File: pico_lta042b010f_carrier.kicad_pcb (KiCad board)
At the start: 2 copper layers, 100 x 52 mm, 31 parts, among them J1 LTA042B010F_FFC_36P_0.5mm, J2 USB-C 5V INPUT, J3 CCFL_INVERTER_13V8, U1 RaspberryPi_Pico_2W, U3 MC34063AD

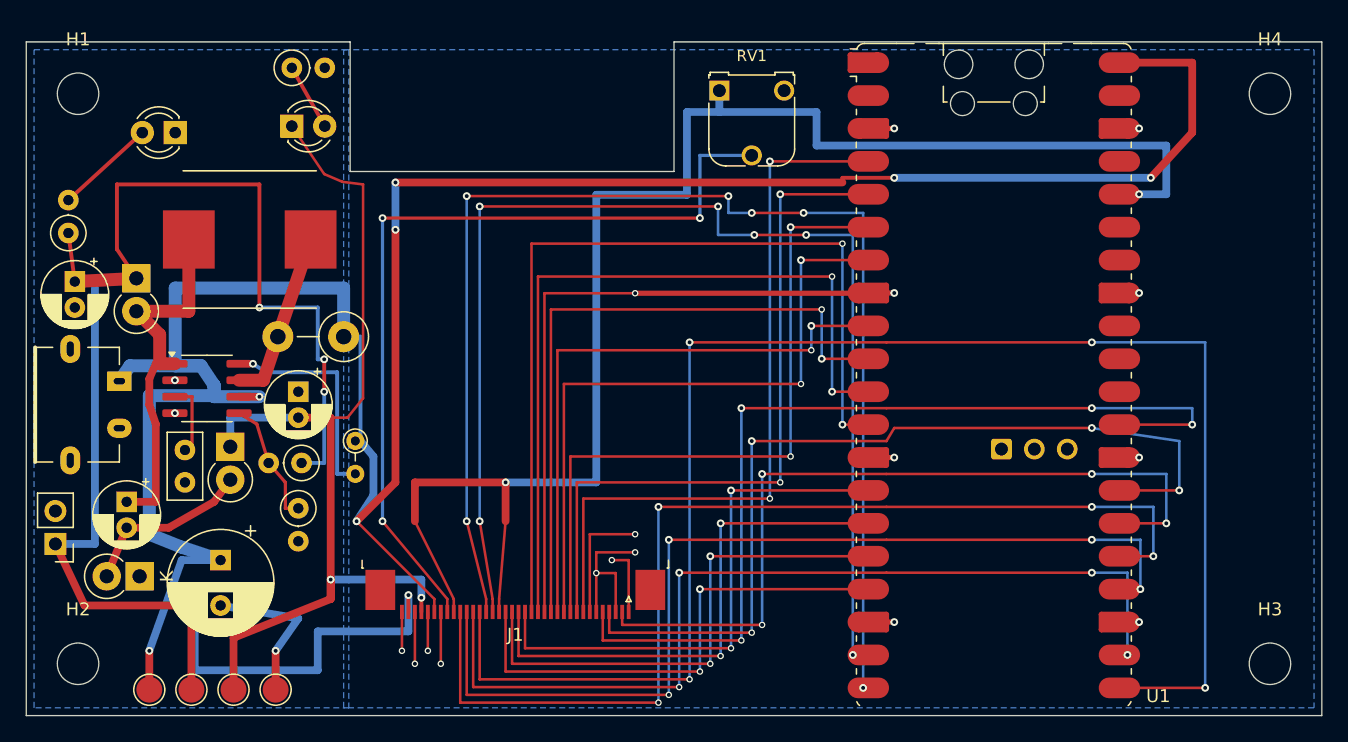
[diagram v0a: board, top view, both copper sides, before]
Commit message: Tighten PCB design rules and edge margins
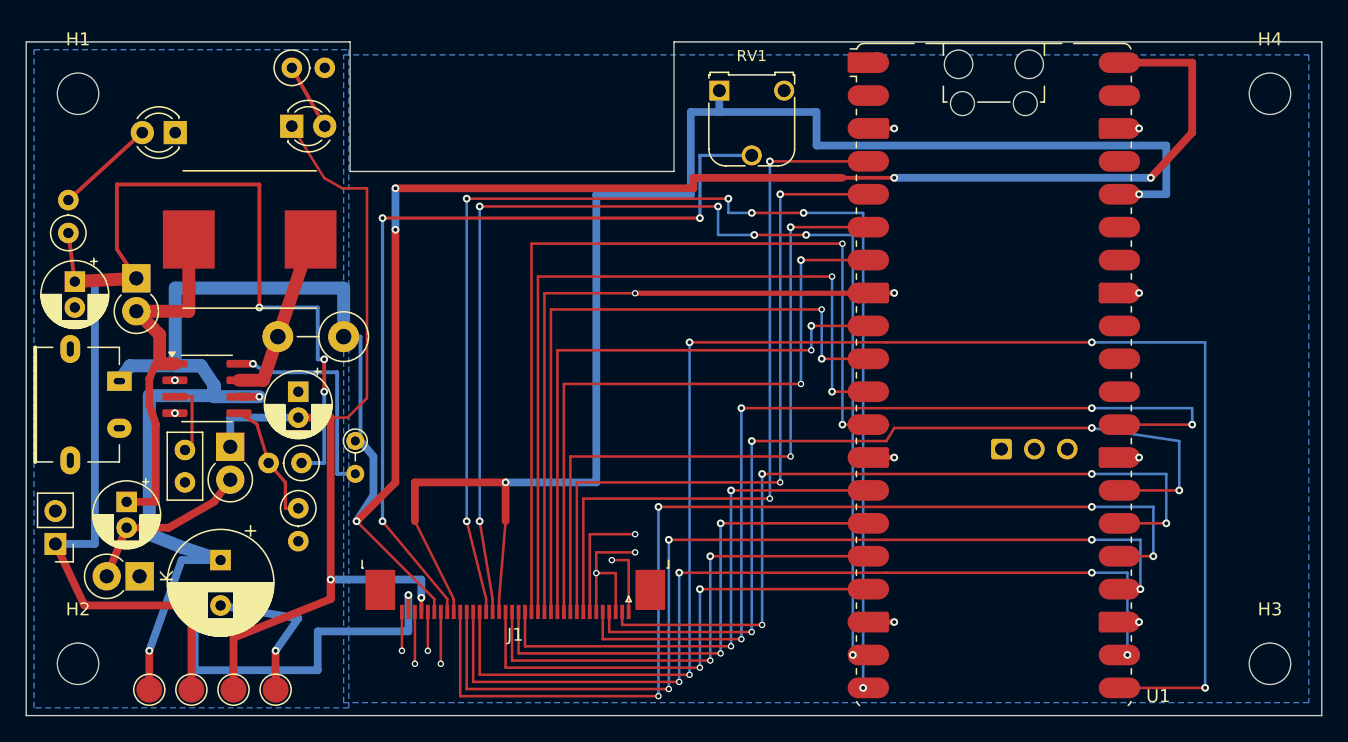
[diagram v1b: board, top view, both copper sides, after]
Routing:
- net LCD_R0: track 82.0 -> 81.0 mm
- net LCD_R1: track 75.8 -> 74.9 mm
- net LCD_R2: track 72.1 -> 71.3 mm
- net LCD_R3: track 120.5 -> 119.8 mm
- net LCD_G0: track 39.0 -> 38.4 mm
- net -13V8: track 76.9 -> 77.4 mm
- net LCD_G1: track 39.8 -> 39.3 mm
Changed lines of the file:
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@@
 	)
 	(segment
-		(start 63 10.85)
-		(end 63 10.49)
-		(width 0.3)
+		(start 28.5 11.3)
+		(end 51.5 11.3)
+		(width 0.6)
+		(layer "F.Cu")
+		(net 2)
+	)
+	(segment
+		(start 51.5 11.3)
+		(end 51.5 10.49)
+		(width 0.6)
 		(layer "F.Cu")
 		(net 2)
@@
 	)
 	(segment
-		(start 28.5 10.85)
-		(end 63 10.85)
+		(start 51.5 10.49)
+		(end 63 10.49)
 		(width 0.6)
 		(layer "F.Cu")
@@
 	)
 	(via
-		(at 28.5 10.85)
+		(at 28.5 11.3)
 		(size 0.6)
 		(drill 0.3)
@@
 	(segment
 		(start 28.5 14.5)
-		(end 28.5 10.85)
+		(end 28.5 11.3)
 		(width 0.6)
 		(layer "B.Cu")
@@
 	)
 	(segment
-		(start 24.4 10.8)
-		(end 23 10.2)
+		(start 24.4 11.3)
+		(end 23 10.5)
 		(width 0.2)
 		(layer "F.Cu")
@@
 	)
 	(segment
-		(start 23 10.2)
+		(start 23 10.5)
 		(end 20.5 6.5)
 		(width 0.2)
@@
 	)
 	(segment
-		(start 26 11)
-		(end 24.4 10.8)
+		(start 26.3 11.3)
+		(end 24.4 11.3)
 		(width 0.2)
 		(layer "F.Cu")
@@
 	(segment
 		(start 24.8 29)
-		(end 26 27.5)
+		(end 26.3 27.5)
 		(width 0.2)
 		(layer "F.Cu")
@@
 	)
 	(segment
-		(start 26 27.5)
-		(end 26 11)
+		(start 26.3 27.5)
+		(end 26.3 11.3)
 		(width 0.2)
 		(layer "F.Cu")
@@
 	(segment
 		(start 44 11.8)
-		(end 51 11.8)
+		(end 51.3 11.8)
 		(width 0.6)
 		(layer "B.Cu")
@@
 	)
 	(segment
-		(start 51 5.41)
+		(start 51.3 5.41)
 		(end 53.5 5.41)
 		(width 0.6)
@@
 	)
 	(segment
-		(start 51 11.8)
-		(end 51 5.41)
+		(start 51.3 11.8)
+		(end 51.3 5.41)
 		(width 0.6)
 		(layer "B.Cu")
@@
 	)
 	(segment
-		(start 45 45.6)
-		(end 56 45.6)
+		(start 45 45.55)
+		(end 56 45.55)
 		(width 0.2)
 		(layer "F.Cu")
@@
 	(segment
 		(start 45 44)
-		(end 45 45.6)
+		(end 45 45.55)
 		(width 0.2)
 		(layer "F.Cu")
@@
 	)
 	(via
-		(at 56 45.6)
+		(at 56 45.55)
 		(size 0.5)
 		(drill 0.3)
@@
 	)
 	(segment
-		(start 56 45.6)
+		(start 56 45.55)
 		(end 56 30.81)
 		(width 0.2)
@@
 	)
 	(segment
-		(start 44.5 46.2)
-		(end 55.2 46.2)
+		(start 44.5 46.1)
+		(end 55.2 46.1)
 		(width 0.2)
 		(layer "F.Cu")
@@
 	(segment
 		(start 44.5 44)
-		(end 44.5 46.2)
+		(end 44.5 46.1)
 		(width 0.2)
 		(layer "F.Cu")
@@
 	)
 	(via
-		(at 55.2 46.2)
+		(at 55.2 46.1)
 		(size 0.5)
 		(drill 0.3)
@@
 	)
 	(segment
-		(start 55.2 46.2)
+		(start 55.2 46.1)
 		(end 55.2 28.27)
 		(width 0.2)
@@
 	)
 	(segment
-		(start 38.5 46.8)
-		(end 54.4 46.8)
+		(start 38.5 46.65)
+		(end 54.4 46.65)
 		(width 0.2)
 		(layer "F.Cu")
@@
 	(segment
 		(start 38.5 44)
-		(end 38.5 46.8)
+		(end 38.5 46.65)
 		(width 0.2)
 		(layer "F.Cu")
@@
 	)
 	(via
-		(at 54.4 46.8)
+		(at 54.4 46.65)
 		(size 0.5)
 		(drill 0.3)
@@
 	)
 	(segment
-		(start 54.4 46.8)
+		(start 54.4 46.65)
 		(end 54.4 34.62)
 		(width 0.2)
@@
 	)
 	(segment
-		(start 38 47.4)
-		(end 53.6 47.4)
+		(start 38 47.2)
+		(end 53.6 47.2)
 		(width 0.2)
 		(layer "F.Cu")
@@
 	(segment
 		(start 38 44)
-		(end 38 47.4)
+		(end 38 47.2)
 		(width 0.2)
 		(layer "F.Cu")
@@
 	)
 	(via
-		(at 53.6 47.4)
+		(at 53.6 47.2)
 		(size 0.5)
 		(drill 0.3)
@@
 	)
 	(segment
-		(start 53.6 47.4)
+		(start 53.6 47.2)
 		(end 53.6 37.16)
 		(width 0.2)
@@
 	)
 	(segment
-		(start 37.5 48)
-		(end 52.8 48)
+		(start 37.5 47.75)
+		(end 52.8 47.75)
 		(width 0.2)
 		(layer "F.Cu")
@@
 	(segment
 		(start 37.5 44)
-		(end 37.5 48)
+		(end 37.5 47.75)
 		(width 0.2)
 		(layer "F.Cu")
@@
 	)
 	(via
-		(at 52.8 48)
+		(at 52.8 47.75)
 		(size 0.5)
 		(drill 0.3)
@@
 	)
 	(segment
-		(start 52.8 48)
+		(start 52.8 47.75)
 		(end 52.8 39.7)
 		(width 0.2)
@@
 	(segment
 		(start 37 44)
-		(end 37 48.6)
+		(end 37 48.3)
 		(width 0.2)
 		(layer "F.Cu")
@@
 	)
 	(segment
-		(start 37 48.6)
-		(end 52 48.6)
+		(start 37 48.3)
+		(end 52 48.3)
 		(width 0.2)
 		(layer "F.Cu")
@@
 	)
 	(via
-		(at 52 48.6)
+		(at 52 48.3)
 		(size 0.5)
 		(drill 0.3)
@@
 	)
 	(segment
-		(start 52 48.6)
+		(start 52 48.3)
 		(end 52 42.24)
 		(width 0.2)
@@
 	)
 	(segment
-		(start 34 11.9)
-		(end 54.2 11.9)
+		(start 34 12.1)
+		(end 54.2 12.1)
 		(width 0.2)
 		(layer "F.Cu")
@@
 	)
 	(via
-		(at 34 11.9)
+		(at 34 12.1)
 		(size 0.6)
 		(drill 0.3)
@@
 	)
 	(via
-		(at 54.2 11.9)
+		(at 54.2 12.1)
 		(size 0.6)
 		(drill 0.3)
@@
 	)
 	(segment
-		(start 54.2 11.9)
+		(start 54.2 12.1)
 		(end 54.2 13.2)
 		(width 0.2)
@@
 	(segment
 		(start 34 37)
-		(end 34 11.9)
+		(end 34 12.1)
 		(width 0.2)
 		(layer "B.Cu")
@@
 	(segment
 		(start 35 44)
-		(end 35 49.2)
+		(end 35 48.85)
 		(width 0.2)
 		(layer "F.Cu")
@@
 	)
 	(segment
-		(start 35 49.2)
-		(end 51.2 49.2)
+		(start 35 48.85)
+		(end 51.2 48.85)
 		(width 0.2)
 		(layer "F.Cu")
@@
 	)
 	(via
-		(at 51.2 49.2)
+		(at 51.2 48.85)
 		(size 0.5)
 		(drill 0.3)
@@
 	)
 	(segment
-		(start 51.2 49.2)
+		(start 51.2 48.85)
 		(end 51.2 23.19)
 		(width 0.2)
@@
 	(segment
 		(start 34.5 44)
-		(end 34.5 49.8)
+		(end 34.5 49.4)
 		(width 0.2)
 		(layer "F.Cu")
@@
 	)
 	(segment
-		(start 34.5 49.8)
-		(end 50.4 49.8)
+		(start 34.5 49.4)
+		(end 50.4 49.4)
 		(width 0.2)
 		(layer "F.Cu")
@@
 	)
 	(via
-		(at 50.4 49.8)
+		(at 50.4 49.4)
 		(size 0.5)
 		(drill 0.3)
@@
 	)
 	(segment
-		(start 50.4 49.8)
+		(start 50.4 49.4)
 		(end 50.4 40.97)
 		(width 0.2)
@@
 	(segment
 		(start 34 44)
-		(end 34 50.4)
+		(end 34 49.95)
 		(width 0.2)
 		(layer "F.Cu")
@@
 	)
 	(segment
-		(start 34 50.4)
-		(end 49.6 50.4)
+		(start 34 49.95)
+		(end 49.6 49.95)
 		(width 0.2)
 		(layer "F.Cu")
@@
 	)
 	(via
-		(at 49.6 50.4)
+		(at 49.6 49.95)
 		(size 0.5)
 		(drill 0.3)
@@
 	)
 	(segment
-		(start 49.6 50.4)
+		(start 49.6 49.95)
 		(end 49.6 38.43)
 		(width 0.2)
@@
 	)
 	(segment
-		(start 33.5 51)
-		(end 48.8 51)
+		(start 33.5 50.5)
+		(end 48.8 50.5)
 		(width 0.2)
 		(layer "F.Cu")
@@
 	(segment
 		(start 33.5 44)
-		(end 33.5 51)
+		(end 33.5 50.5)
 		(width 0.2)
 		(layer "F.Cu")
@@
 	)
 	(via
-		(at 48.8 51)
+		(at 48.8 50.5)
 		(size 0.5)
 		(drill 0.3)
@@
 	)
 	(segment
-		(start 48.8 51)
+		(start 48.8 50.5)
 		(end 48.8 35.89)
 		(width 0.2)
@@
 		(polygon
 			(pts
-				(xy 24.5 0.6) (xy 99.4 0.6) (xy 99.4 51.4) (xy 24.5 51.4)
+				(xy 24.5 1) (xy 99 1) (xy 99 51) (xy 24.5 51)
 			)
 		)

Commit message: Add dual-layer thermal ground pours
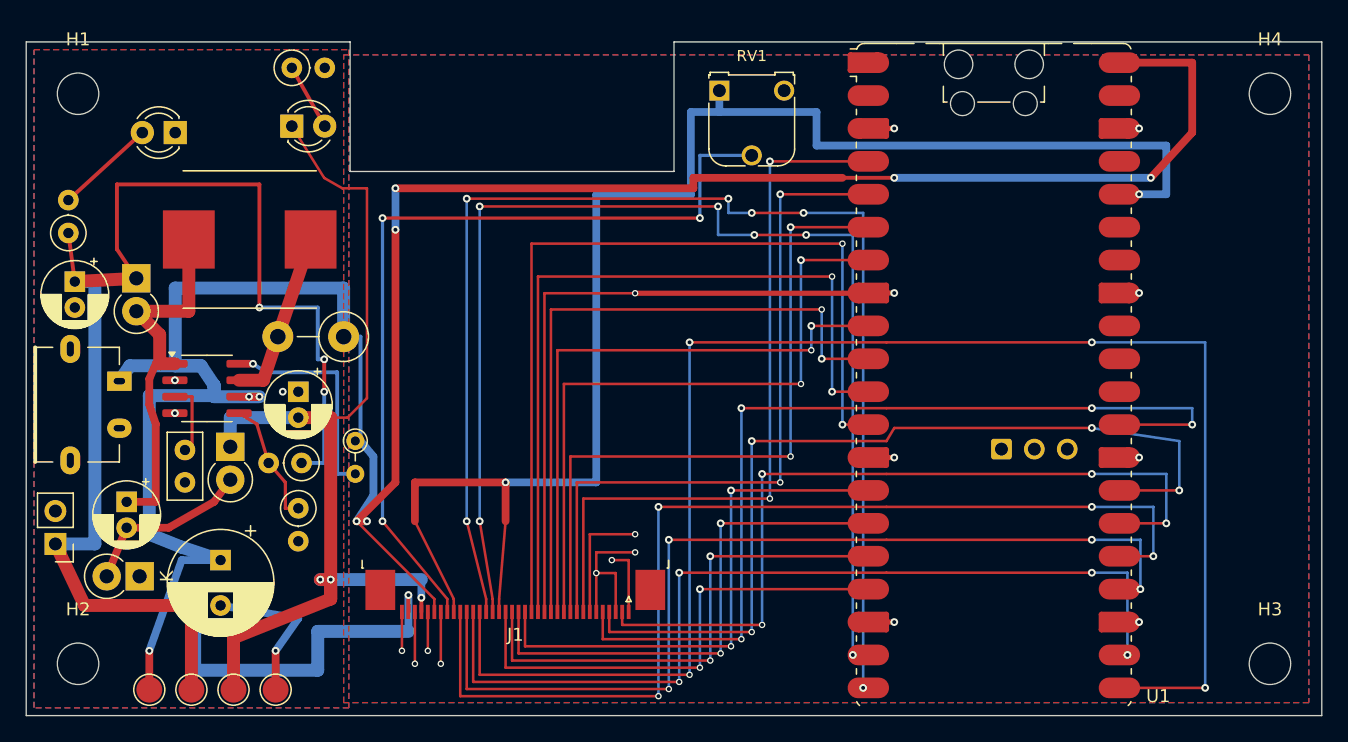
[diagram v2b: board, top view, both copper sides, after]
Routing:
- net +5V: track 203.2 -> 205.6 mm, vias 7 -> 9
- net +13V8: track 130.6 -> 132.2 mm, vias 5 -> 6
- net -13V8: track 77.4 -> 79.0 mm, vias 2 -> 3
- net GND: vias 20 -> 21
- added copper zone on F.Cu, net GND
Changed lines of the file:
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@@
+	)
+	(via
+		(at 19.8 27)
+		(size 0.6)
+		(drill 0.3)
+		(layers "F.Cu" "B.Cu")
+		(net 1)
 	)
 	(via
@@
 	)
 	(segment
+		(start 18 27.385)
+		(end 17.2 27.385)
+		(width 0.6)
+		(layer "F.Cu")
+		(net 2)
+	)
+	(segment
 		(start 28.5 11.3)
 		(end 51.5 11.3)
@@
 		(start 18 27.385)
 		(end 16.425 27.385)
+		(width 0.6)
+		(layer "F.Cu")
+		(net 2)
+	)
+	(segment
+		(start 25.5 37)
+		(end 26.3 37)
 		(width 0.6)
 		(layer "F.Cu")
@@
 	)
 	(via
+		(at 17.2 27.385)
+		(size 0.6)
+		(drill 0.3)
+		(layers "F.Cu" "B.Cu")
+		(net 2)
+	)
+	(via
 		(at 86.8 10.49)
+		(size 0.6)
+		(drill 0.3)
+		(layers "F.Cu" "B.Cu")
+		(net 2)
+	)
+	(via
+		(at 26.3 37)
 		(size 0.6)
 		(drill 0.3)
@@
 	)
 	(segment
+		(start 25.5 37)
+		(end 26.3 37)
+		(width 0.6)
+		(layer "B.Cu")
+		(net 2)
+	)
+	(segment
 		(start 13.5 25)
 		(end 14.5 26.5)
@@
 		(start 4.5 43.5)
 		(end 12.75 43.5)
-		(width 0.6)
+		(width 1)
 		(layer "F.Cu")
 		(net 3)
@@
 	)
 	(segment
+		(start 13 42.7)
+		(end 12.2 42.7)
+		(width 1)
+		(layer "F.Cu")
+		(net 3)
+	)
+	(segment
 		(start 3.75 18.5)
 		(end 3.25 14.75)
@@
 		(start 13 42.7)
 		(end 12.75 43.5)
-		(width 0.6)
+		(width 1)
 		(layer "F.Cu")
 		(net 3)
@@
 		(start 2.25 38.75)
 		(end 4.5 43.5)
-		(width 0.6)
+		(width 1)
 		(layer "F.Cu")
 		(net 3)
@@
 		(start 12.75 43.5)
 		(end 12.75 50)
-		(width 0.6)
+		(width 1)
 		(layer "F.Cu")
 		(net 3)
@@
 	)
 	(via
+		(at 12.2 42.7)
+		(size 0.6)
+		(drill 0.3)
+		(layers "F.Cu" "B.Cu")
+		(net 3)
+	)
+	(via
 		(at 18 20.5)
 		(size 0.6)
@@
 		(start 13 48.5)
 		(end 13 42.7)
-		(width 0.6)
+		(width 1)
 		(layer "B.Cu")
 		(net 3)
@@
 		(start 29.5 45.5)
 		(end 22.5 45.5)
-		(width 0.6)
+		(width 1)
+		(layer "B.Cu")
+		(net 3)
+	)
+	(segment
+		(start 13 42.7)
+		(end 12.2 42.7)
+		(width 1)
 		(layer "B.Cu")
 		(net 3)
@@
 		(start 5.3 38.75)
 		(end 2.25 38.75)
-		(width 0.6)
+		(width 1)
 		(layer "B.Cu")
 		(net 3)
@@
 		(start 3.75 18.5)
 		(end 5.3 18.5)
-		(width 0.6)
+		(width 1)
 		(layer "B.Cu")
 		(net 3)
@@
 		(start 22.5 45.5)
 		(end 22.5 48.5)
-		(width 0.6)
+		(width 1)
 		(layer "B.Cu")
 		(net 3)
@@
 		(start 5.3 18.5)
 		(end 5.3 38.75)
-		(width 0.6)
+		(width 1)
 		(layer "B.Cu")
 		(net 3)
@@
 		(start 22.5 48.5)
 		(end 13 48.5)
-		(width 0.6)
+		(width 1)
 		(layer "B.Cu")
 		(net 3)
@@
 		(start 23.5 43)
 		(end 16 46)
-		(width 0.6)
+		(width 1)
 		(layer "F.Cu")
 		(net 4)
@@
 		(start 23.5 29)
 		(end 23.5 43)
-		(width 0.6)
+		(width 1)
 		(layer "F.Cu")
 		(net 4)
@@
 		(start 21 29)
 		(end 23.5 29)
-		(width 0.6)
+		(width 1)
 		(layer "F.Cu")
 		(net 4)
@@
 		(start 16 46)
 		(end 16 50)
-		(width 0.6)
+		(width 1)
+		(layer "F.Cu")
+		(net 4)
+	)
+	(segment
+		(start 23.5 41.5)
+		(end 22.7 41.5)
+		(width 1)
 		(layer "F.Cu")
 		(net 4)
@@
 		(start 23.5 41.5)
 		(end 23.5 43)
-		(width 0.6)
+		(width 1)
 		(layer "F.Cu")
 		(net 4)
@@
 	)
 	(via
+		(at 22.7 41.5)
+		(size 0.6)
+		(drill 0.3)
+		(layers "F.Cu" "B.Cu")
+		(net 4)
+	)
+	(via
 		(at 23.5 41.5)
 		(size 0.6)
@@
 		(start 15.75 31.25)
 		(end 15.75 29)
-		(width 0.6)
+		(width 1)
 		(layer "B.Cu")
 		(net 4)
@@
 		(start 15.75 29)
 		(end 21 29)
-		(width 0.6)
+		(width 1)
 		(layer "B.Cu")
 		(net 4)
@@
 		(start 30.5 41.5)
 		(end 23.5 41.5)
-		(width 0.6)
+		(width 1)
+		(layer "B.Cu")
+		(net 4)
+	)
+	(segment
+		(start 23.5 41.5)
+		(end 22.7 41.5)
+		(width 1)
 		(layer "B.Cu")
 		(net 4)
@@
 		(net 1)
 		(net_name "GND")
-		(layer "B.Cu")
-		(name "LOGIC_GND")
+		(layer "F.Cu")
+		(name "POWER_STAGE_GND_F")
 		(hatch edge 0.5)
-		(connect_pads yes
+		(connect_pads
 			(clearance 0.3)
 		)
@@
 		(filled_areas_thickness no)
 		(fill yes
-			(thermal_gap 0.5)
-			(thermal_bridge_width 0.5)
+			(thermal_gap 0.3)
+			(thermal_bridge_width 0.3)
+		)
+		(polygon
+			(pts
+				(xy 0.6 0.6) (xy 24.9 0.6) (xy 24.9 51.4) (xy 0.6 51.4)
+			)
+		)
+	)
+	(zone
+		(net 1)
+		(net_name "GND")
+		(layer "F.Cu")
+		(name "LOGIC_GND_F")
+		(hatch edge 0.5)
+		(connect_pads
+			(clearance 0.3)
+		)
+		(min_thickness 0.25)
+		(filled_areas_thickness no)
+		(fill yes
+			(thermal_gap 0.3)
+			(thermal_bridge_width 0.3)
 		)
 		(polygon
@@
 		(net_name "GND")
 		(layer "B.Cu")
-		(name "POWER_STAGE_GND")
+		(name "LOGIC_GND")
 		(hatch edge 0.5)
-		(connect_pads yes
+		(connect_pads
 			(clearance 0.3)
 		)
@@
 		(filled_areas_thickness no)
 		(fill yes
-			(thermal_gap 0.5)
-			(thermal_bridge_width 0.5)
+			(thermal_gap 0.3)
+			(thermal_bridge_width 0.3)
 		)
 		(polygon
+			(pts
+				(xy 24.5 1) (xy 99 1) (xy 99 51) (xy 24.5 51)
+			)
+		)
+	)
+	(zone
+		(net 1)
+		(net_name "GND")
+		(layer "B.Cu")
+		(name "POWER_STAGE_GND")
+		(hatch edge 0.5)
+		(connect_pads
+			(clearance 0.3)
+		)
+		(min_thickness 0.25)
+		(filled_areas_thickness no)
+		(fill yes
+			(thermal_gap 0.3)
+			(thermal_bridge_width 0.3)
+		)
+		(polygon
